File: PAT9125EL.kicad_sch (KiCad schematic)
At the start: 9 parts, among them J1 Conn_01x06_Socket, U1 PAT9125EL

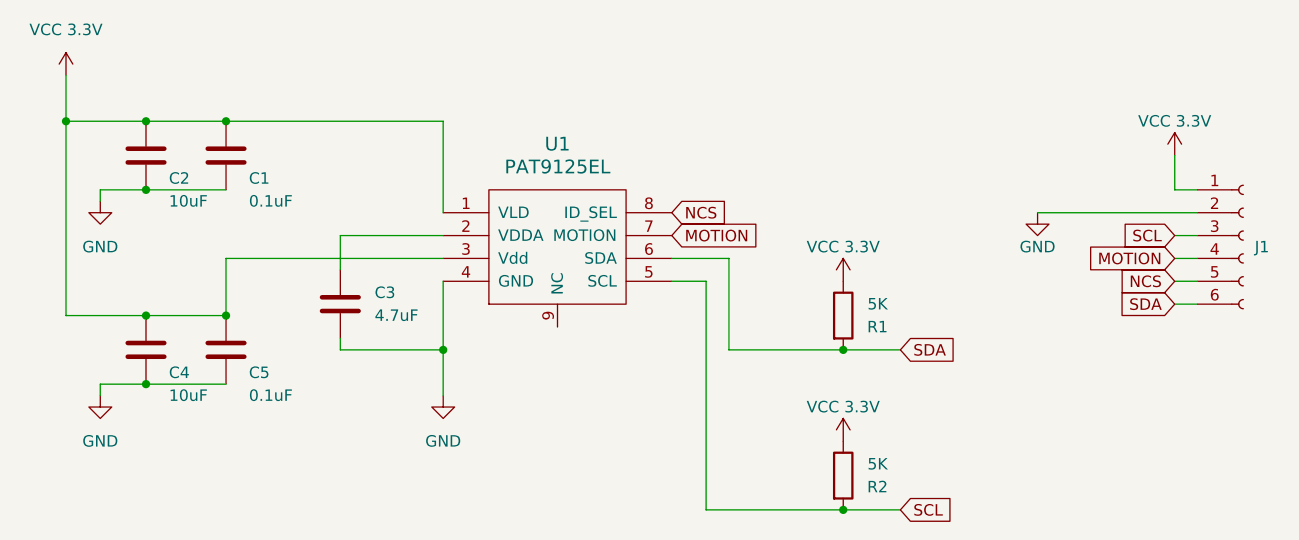
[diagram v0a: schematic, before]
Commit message: shorten 1.5mm
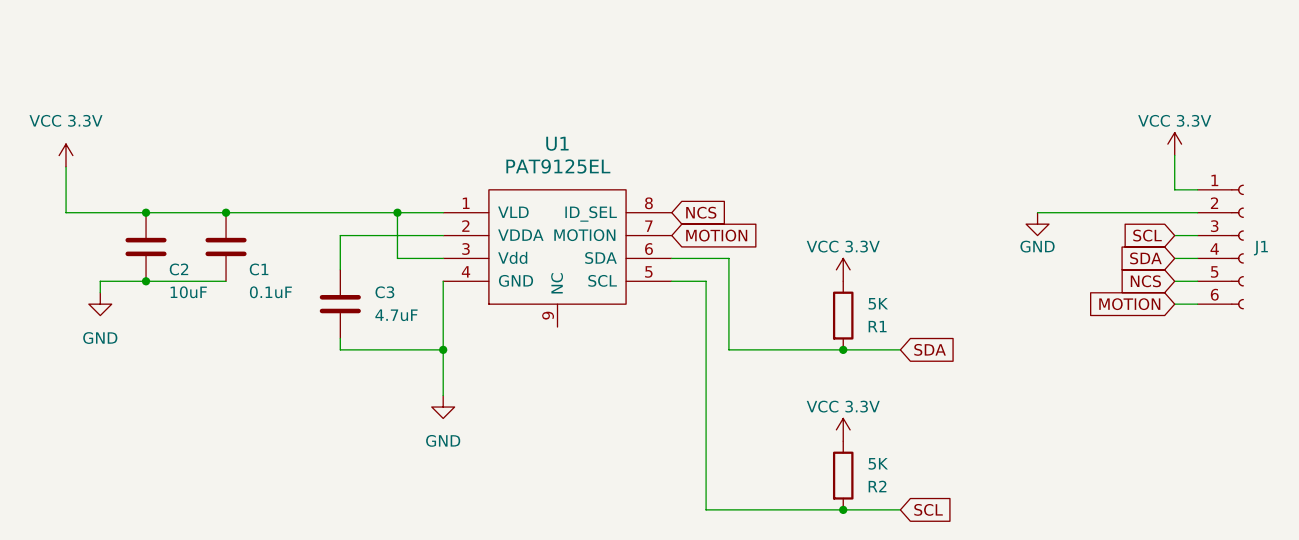
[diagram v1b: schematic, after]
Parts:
- removed C4: 10uF, Capacitor_SMD:C_0402_1005Metric, symbol Device:C
- removed C5: 0.1uF, Capacitor_SMD:C_0402_1005Metric, symbol Device:C
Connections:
- net MOTION: now also J1.6 (Pin_6); no longer J1.4 (Pin_4)
- net SDA: now also J1.4 (Pin_4); no longer J1.6 (Pin_6)
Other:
- moved on the sheet: C1, C2
